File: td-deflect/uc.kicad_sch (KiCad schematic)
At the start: 17 parts, among them J4 Conn_ARM_JTAG_SWD_10, J6 Conn_01x06_Male, U12 LM1117-5.0, U2 STM32G474xx, U3 INA193, U4 TPS70933, X1 SG-8002CA

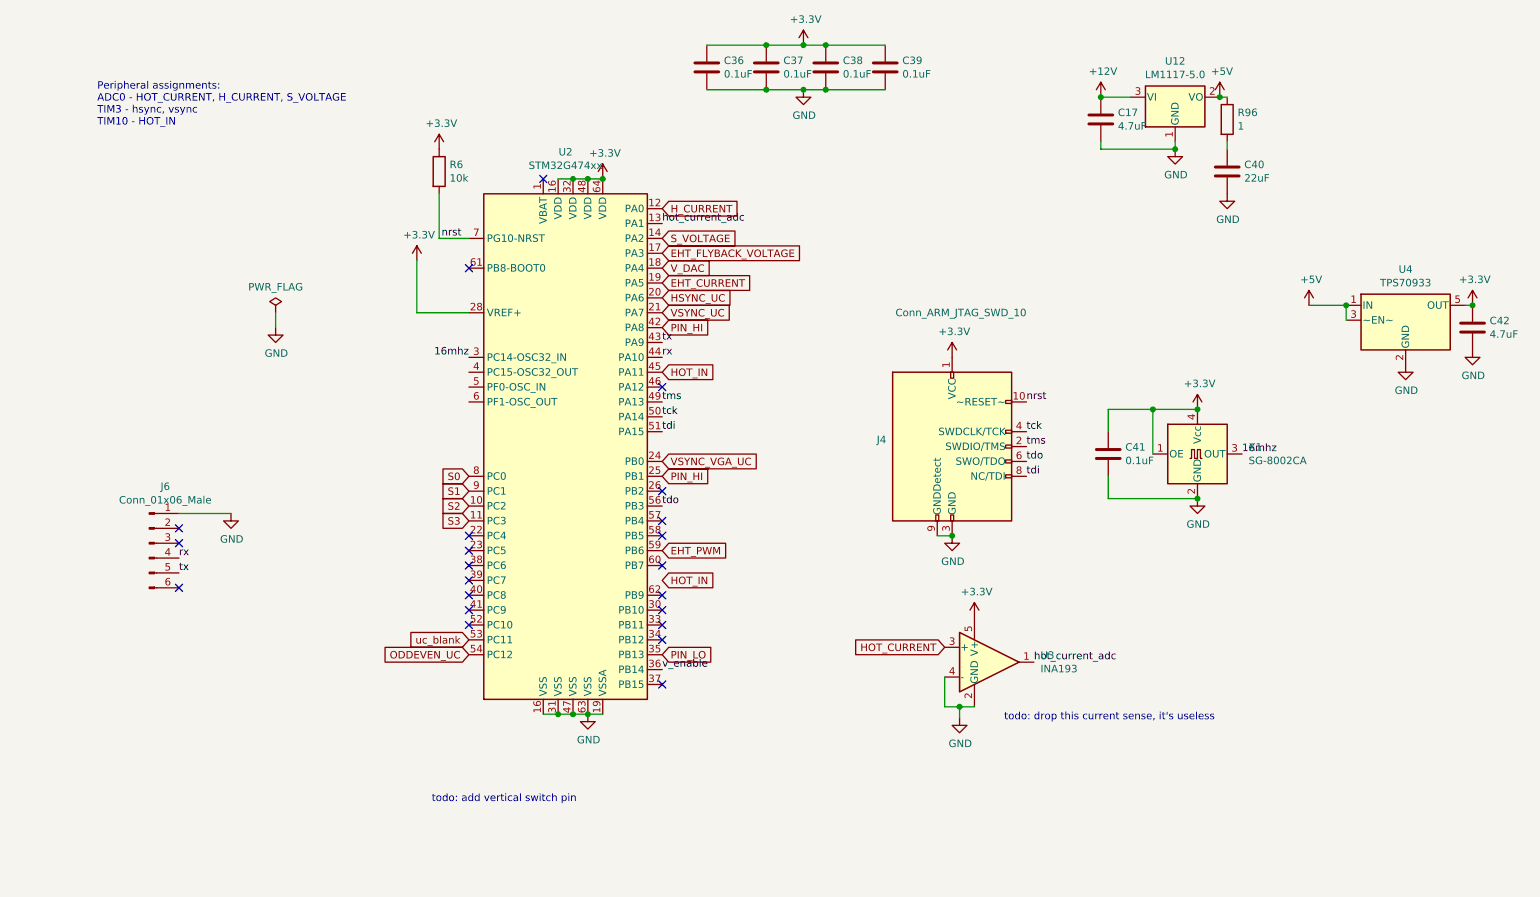
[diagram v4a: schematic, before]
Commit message: add hv protect and more sense lines
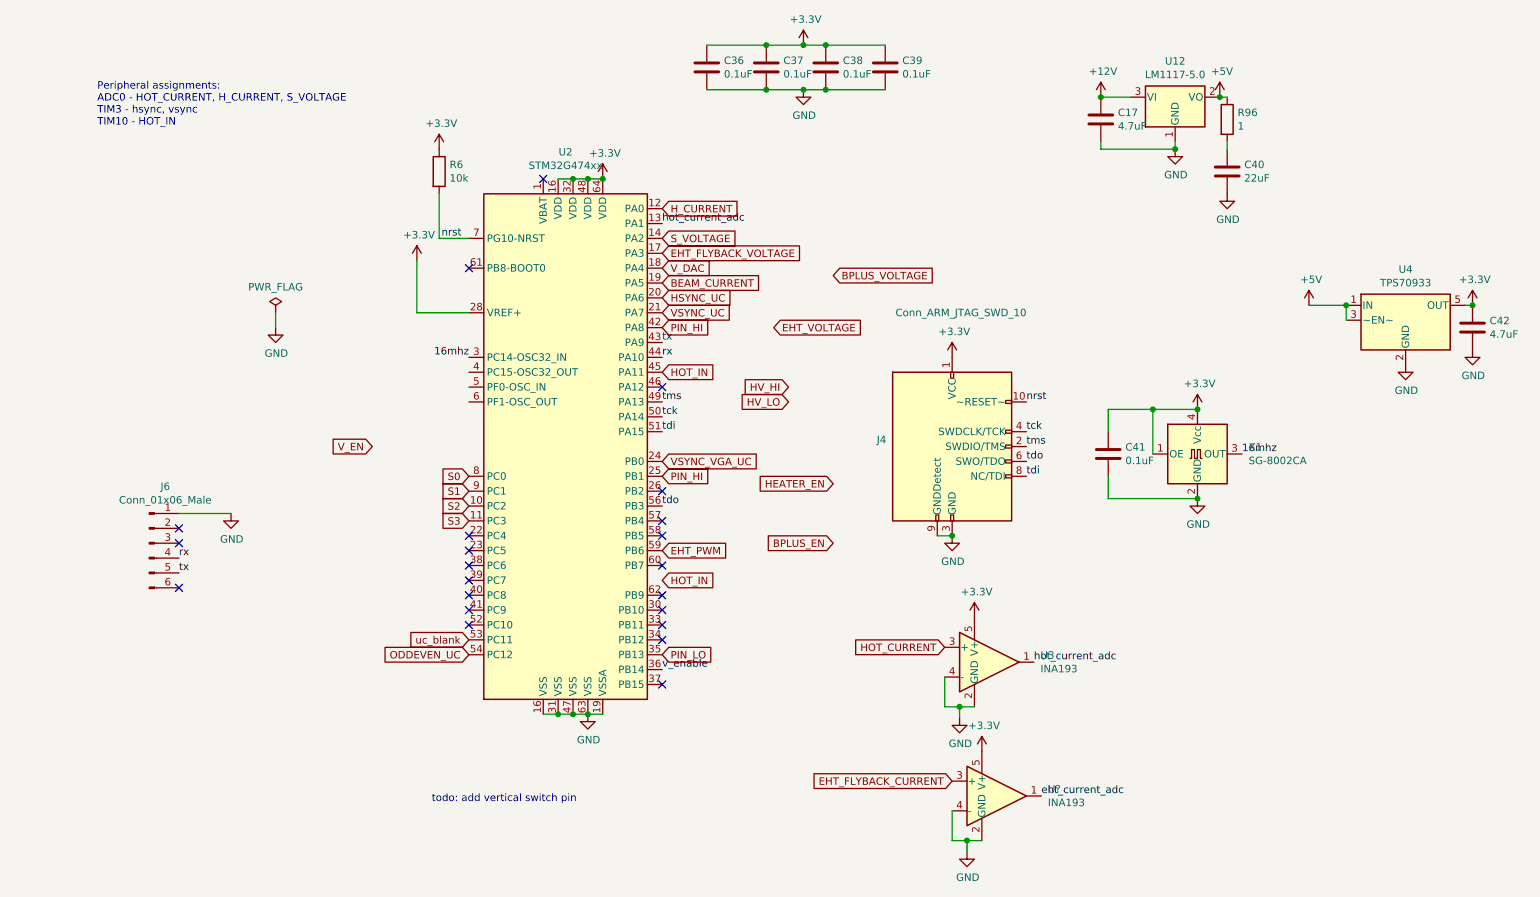
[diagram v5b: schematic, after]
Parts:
- added U?: INA193, Package_TO_SOT_SMD:SOT-23-5, symbol Amplifier_Current:INA193
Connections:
- net EHT_CURRENT is gone; now on net GND: U2.19 (VSSA)
- net +3V3: now also U?.5 (V+)
- net GND: now also U?.2 (GND), U?.4 (-)
- new net BEAM_CURRENT: U2.19 (VSSA)
- new net EHT_FLYBACK_CURRENT: U?.3 (+)
- new net eht_current_adc: U?.1
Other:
- note removed: "todo: drop this current sense, it's useless"
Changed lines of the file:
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@@
   (junction (at 151.13 21.59) (diameter 1.016) (color 0 0 0 0)
+  )
+  (junction (at 185.42 157.48) (diameter 1.016) (color 0 0 0 0)
   )
   (junction (at 157.48 29.21) (diameter 1.016) (color 0 0 0 0)
@@
     (stroke (width 0) (type solid) (color 0 0 0 0))
   )
+  (wire (pts (xy 185.42 159.385) (xy 185.42 157.48))
+    (stroke (width 0) (type solid) (color 0 0 0 0))
+  )
   (wire (pts (xy 184.15 136.525) (xy 184.15 134.62))
     (stroke (width 0) (type solid) (color 0 0 0 0))
@@
   )
   (wire (pts (xy 91.44 58.42) (xy 91.44 67.31))
+    (stroke (width 0) (type solid) (color 0 0 0 0))
+  )
+  (wire (pts (xy 182.88 152.4) (xy 182.88 157.48))
     (stroke (width 0) (type solid) (color 0 0 0 0))
   )
@@
     (stroke (width 0) (type solid) (color 0 0 0 0))
   )
+  (wire (pts (xy 185.42 157.48) (xy 187.96 157.48))
+    (stroke (width 0) (type solid) (color 0 0 0 0))
+  )
   (wire (pts (xy 224.79 83.82) (xy 217.17 83.82))
     (stroke (width 0) (type solid) (color 0 0 0 0))
@@
   )
   (wire (pts (xy 209.55 87.63) (xy 209.55 83.82))
+    (stroke (width 0) (type solid) (color 0 0 0 0))
+  )
+  (wire (pts (xy 182.88 157.48) (xy 185.42 157.48))
     (stroke (width 0) (type solid) (color 0 0 0 0))
   )
@@
     (effects (font (size 1.27 1.27)) (justify left bottom))
   )
-  (text "todo: drop this current sense, it's useless" (at 191.77 137.16 0)
-    (effects (font (size 1.27 1.27)) (justify left bottom))
-  )
   (label "tx" (at 50.8 111.76 0)
     (effects (font (size 1.27 1.27)) (justify left bottom))
@@
   )
   (label "tdi" (at 195.58 95.25 0)
+    (effects (font (size 1.27 1.27)) (justify left bottom))
+  )
+  (label "eht_current_adc" (at 198.12 149.86 0)
     (effects (font (size 1.27 1.27)) (justify left bottom))
   )
@@
     )
   )
+  (global_label "HV_HI" (shape input) (at 154.94 80.01 180) (fields_autoplaced)
+    (effects (font (size 1.27 1.27)) (justify right))
+    (property "Intersheet References" "${INTERSHEET_REFS}" (id 0) (at 147.2939 79.9306 0)
+      (effects (font (size 1.27 1.27)) (justify right) hide)
+    )
+  )
   (global_label "HOT_IN" (shape input) (at 133.35 77.47 0) (fields_autoplaced)
     (effects (font (size 1.27 1.27)) (justify left))
@@
     )
   )
+  (global_label "BEAM_CURRENT" (shape input) (at 133.35 62.23 0) (fields_autoplaced)
+    (effects (font (size 1.27 1.27)) (justify left))
+    (property "Intersheet References" "${INTERSHEET_REFS}" (id 0) (at 150.1885 62.1506 0)
+      (effects (font (size 1.27 1.27)) (justify left) hide)
+    )
+  )
   (global_label "HSYNC_UC" (shape input) (at 133.35 64.77 0) (fields_autoplaced)
     (effects (font (size 1.27 1.27)) (justify left))
@@
     (property "Intersheet References" "${INTERSHEET_REFS}" (id 0) (at 0 0 0)
       (effects (font (size 1.27 1.27)) hide)
+    )
+  )
+  (global_label "HEATER_EN" (shape input) (at 162.56 96.52 180) (fields_autoplaced)
+    (effects (font (size 1.27 1.27)) (justify right))
+    (property "Intersheet References" "${INTERSHEET_REFS}" (id 0) (at 149.8339 96.4406 0)
+      (effects (font (size 1.27 1.27)) (justify right) hide)
     )
   )
@@
     )
   )
+  (global_label "V_EN" (shape input) (at 83.82 90.17 180) (fields_autoplaced)
+    (effects (font (size 1.27 1.27)) (justify right))
+    (property "Intersheet References" "${INTERSHEET_REFS}" (id 0) (at 76.9601 90.2494 0)
+      (effects (font (size 1.27 1.27)) (justify right) hide)
+    )
+  )
   (global_label "PIN_LO" (shape input) (at 133.35 125.73 0) (fields_autoplaced)
     (effects (font (size 1.27 1.27)) (justify left))
@@
     (property "Intersheet References" "${INTERSHEET_REFS}" (id 0) (at 0 0 0)
       (effects (font (size 1.27 1.27)) hide)
+    )
+  )
+  (global_label "BPLUS_VOLTAGE" (shape input) (at 162.56 60.96 0) (fields_autoplaced)
+    (effects (font (size 1.27 1.27)) (justify left))
+    (property "Intersheet References" "${INTERSHEET_REFS}" (id 0) (at 179.8823 60.8806 0)
+      (effects (font (size 1.27 1.27)) (justify left) hide)
     )
   )
@@
     )
   )
-  (global_label "EHT_CURRENT" (shape input) (at 133.35 62.23 0) (fields_autoplaced)
-    (effects (font (size 1.27 1.27)) (justify left))
-    (property "Intersheet References" "${INTERSHEET_REFS}" (id 0) (at 0 0 0)
-      (effects (font (size 1.27 1.27)) hide)
+  (global_label "HV_LO" (shape input) (at 154.94 82.55 180) (fields_autoplaced)
+    (effects (font (size 1.27 1.27)) (justify right))
+    (property "Intersheet References" "${INTERSHEET_REFS}" (id 0) (at 146.8706 82.4706 0)
+      (effects (font (size 1.27 1.27)) (justify right) hide)
+    )
+  )
+  (global_label "EHT_FLYBACK_CURRENT" (shape input) (at 182.88 147.32 180) (fields_autoplaced)
+    (effects (font (size 1.27 1.27)) (justify right))
+    (property "Intersheet References" "${INTERSHEET_REFS}" (id 0) (at 158.482 147.3994 0)
+      (effects (font (size 1.27 1.27)) (justify right) hide)
     )
   )
@@
     )
   )
+  (global_label "BPLUS_EN" (shape input) (at 162.56 106.68 180) (fields_autoplaced)
+    (effects (font (size 1.27 1.27)) (justify right))
+    (property "Intersheet References" "${INTERSHEET_REFS}" (id 0) (at 150.6806 106.6006 0)
+      (effects (font (size 1.27 1.27)) (justify right) hide)
+    )
+  )
   (global_label "V_DAC" (shape input) (at 133.35 59.69 0) (fields_autoplaced)
     (effects (font (size 1.27 1.27)) (justify left))
@@
     (property "Intersheet References" "${INTERSHEET_REFS}" (id 0) (at 0 0 0)
       (effects (font (size 1.27 1.27)) hide)
+    )
+  )
+  (global_label "EHT_VOLTAGE" (shape input) (at 152.4 69.85 0) (fields_autoplaced)
+    (effects (font (size 1.27 1.27)) (justify left))
+    (property "Intersheet References" "${INTERSHEET_REFS}" (id 0) (at 167.0613 69.7706 0)
+      (effects (font (size 1.27 1.27)) (justify left) hide)
     )
   )
@@
       (effects (font (size 1.27 1.27)) hide)
     )
+    (pin "1")
+  )
+  (symbol (lib_id "Amplifier_Current:INA193") (at 190.5 149.86 0) (unit 1)
+    (in_bom yes) (on_board yes)
+    (property "Reference" "U?" (id 0) (at 199.2376 148.6916 0)
+      (effects (font (size 1.27 1.27)) (justify left))
+    )
+    (property "Value" "INA193" (id 1) (at 199.2376 151.003 0)
+      (effects (font (size 1.27 1.27)) (justify left))
+    )
+    (property "Footprint" "Package_TO_SOT_SMD:SOT-23-5" (id 2) (at 190.5 149.86 0)
+      (effects (font (size 1.27 1.27)) hide)
+    )
+    (property "Datasheet" "http://www.ti.com/lit/ds/symlink/ina193.pdf" (id 3) (at 190.5 149.86 0)
+      (effects (font (size 1.27 1.27)) hide)
+    )
+    (property "Digikey" "296-26065-1-ND" (id 4) (at 190.5 149.86 0)
+      (effects (font (size 1.27 1.27)) hide)
+    )
+    (pin "1")
+    (pin "2")
+    (pin "3")
+    (pin "4")
+    (pin "5")
+  )
+  (symbol (lib_id "power:GND") (at 185.42 159.385 0) (unit 1)
+    (in_bom yes) (on_board yes)
+    (property "Reference" "#PWR?" (id 0) (at 185.42 165.735 0)
+      (effects (font (size 1.27 1.27)) hide)
+    )
+    (property "Value" "GND" (id 1) (at 185.547 163.7792 0))
+    (property "Footprint" "" (id 2) (at 185.42 159.385 0)
+      (effects (font (size 1.27 1.27)) hide)
+    )
+    (property "Datasheet" "" (id 3) (at 185.42 159.385 0)
+      (effects (font (size 1.27 1.27)) hide)
+    )
+    (pin "1")
+  )
+  (symbol (lib_id "power:+3.3V") (at 187.96 142.24 0) (unit 1)
+    (in_bom yes) (on_board yes)
+    (property "Reference" "#PWR?" (id 0) (at 187.96 146.05 0)
+      (effects (font (size 1.27 1.27)) hide)
+    )
+    (property "Value" "+3.3V" (id 1) (at 188.341 137.8458 0))
+    (property "Footprint" "" (id 2) (at 187.96 142.24 0)
+      (effects (font (size 1.27 1.27)) hide)
+    )
+    (property "Datasheet" "" (id 3) (at 187.96 142.24 0)
+      (effects (font (size 1.27 1.27)) hide)
+    )
